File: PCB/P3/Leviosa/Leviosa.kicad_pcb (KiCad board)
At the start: 2 copper layers, 80 x 80 mm, 54 parts, among them J1 Barrel_Jack, J2 2.54mm 1x03 Spare

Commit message: create PCB initial draft
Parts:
- removed 0R1: DNP, Resistor_SMD:R_0603_1608Metric
- removed Q_noMag1: NCE0110K, Package_TO_SOT_SMD:TO-252-2
- removed R13: 1kΩ, Resistor_SMD:R_0805_2012Metric_Pad1.20x1.40mm_HandSolder
- removed R15: 0Ω, Resistor_SMD:R_0603_1608Metric
- removed TP_noMag1: no_magnet_point_trigger, TestPoint:TestPoint_Pad_D1.5mm
- removed hall_sensor1: SS495A, Connector_PinHeader_2.54mm:PinHeader_1x03_P2.54mm_Vertical
- added C5: 22µF, Capacitor_SMD:C_0805_2012Metric, F.Cu at (66.5, 111.1)
- added C6: 22µF, Capacitor_SMD:C_0805_2012Metric, F.Cu at (76.8, 111.1)
- added C_hall1: 4.7nF, Capacitor_SMD:C_0805_2012Metric_Pad1.18x1.45mm_HandSolder, F.Cu at (92.2, 65.7)
- added R14: 3.9kΩ, Resistor_SMD:R_0603_1608Metric, F.Cu at (92.8, 75.7)
- added R_brake1: 8.2Ω, Resistor_SMD:R_1206_3216Metric, F.Cu at (118.8, 71.7)
- added gate_driver1: MX27517, Package_TO_SOT_SMD:SOT-23-6, F.Cu at (100.5, 71.7)
- added hall1: SS495A, Connector_PinHeader_2.54mm:PinHeader_1x03_P2.54mm_Vertical, F.Cu at (81.2, 68.0)
- added opAmp1: MCP6001R, Package_TO_SOT_SMD:SOT-23-5, F.Cu at (87.0, 67.6)
- C1, C3: value 22µF -> 0.33µF
- Coil1: value 3.7mH -> 7.4mH; footprint Inductor_THT:L_Axial_L5.0mm_D3.6mm_P10.00mm_Horizontal_Murata_BL01RN1A2A2 -> Connector_PinHeader_2.54mm:PinHeader_2x01_P2.54mm_Vertical
- R4: value DNP -> 8.2Ω; footprint Resistor_SMD:R_0603_1608Metric -> Resistor_SMD:R_1206_3216Metric
- R5: footprint Resistor_SMD:R_0603_1608Metric -> Resistor_SMD:R_0805_2012Metric_Pad1.20x1.40mm_HandSolder
- R8: value 1kΩ -> 0Ω
- TP_12V1, TP_Fault1, TP_GND1, TP_Vout1, TP_coilOut1, TP_setPt1: footprint TestPoint:TestPoint_Pad_D1.5mm -> TestPoint:TestPoint_Pad_D1.0mm
- V_reg1: value AMS1117-5.0 -> MC7805BD2TR4G; footprint Package_TO_SOT_SMD:SOT-223-3_TabPin2 -> Package_TO_SOT_SMD:TO-263-2
- comparator1: footprint Package_SO:SOIC-8_5.3x5.3mm_P1.27mm -> Package_SO:SOIC-8_3.9x4.9mm_P1.27mm
- moved H3 140.8 mm to (222.8, 106.6)
- moved H2 138.6 mm to (222.8, 99.3)
- moved FID2 136.0 mm to (223.5, 119.8)
- moved FID3 104.2 mm to (223.5, 122.3)
- moved FID1 102.2 mm to (223.5, 117.2)
- moved H1 87.2 mm to (222.8, 92.1)
- moved TP_5V1 65.4 mm to (66.4, 90.4)
- moved R3 61.1 mm to (112.3, 76.2), turned to 0 degrees
- moved R4 60.1 mm to (91.9, 68.0)
- moved D2 57.1 mm to (108.5, 76.2)
- moved TP_Vout1 56.9 mm to (114.5, 80.1)
- moved D1 52.6 mm to (103.9, 75.6), turned to 0 degrees
- moved R5 48.7 mm to (104.2, 71.8), turned to -90 degrees
- moved TP_GND1 47.9 mm to (81.6, 114.5)
- moved C2 47.5 mm to (99.5, 75.7), turned to 90 degrees
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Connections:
- C_coil1 pad 1: Net-(D_coil1-K) -> /V_out
- Coil1 pad 1: Net-(D_coil1-K) -> /V_out
- Coil1 pad 2: /coil_output -> Net-(Coil1-Pad2)
- D_coil1 pad 1: Net-(D_coil1-K) -> /V_out
- D_coil1 pad 2: /coil_output -> Net-(D_coil1-A)
- Q_setPt1 pad 1: Net-(Q_setPt1-G) -> /gate_driver_out
- Q_setPt1 pad 3: /transistor1_output -> GND
- R10 pad 1: Net-(0R1-Pad1) -> Net-(Coil1-Pad2)
- R4 pad 1: Net-(current_sense1-REF) -> /instrumental_out
- R4 pad 2: /5V -> Net-(comparator1A-+)
- R5 pad 1: GND -> Net-(gate_driver1-OUT)
- R5 pad 2: Net-(current_sense1-REF) -> /gate_driver_out
- R8 pad 1: Net-(Q_setPt1-G) -> /comparator_out
- R8 pad 2: /set_point_trigger -> Net-(gate_driver1-IN+)
- R9 pad 1: /V_out -> /coil_output
- R_shunt1 pad 1: Net-(D_coil1-K) -> Net-(Coil1-Pad2)
- R_shunt1 pad 2: /V_out -> /coil_output
- Servo1 pad 2: GND -> /5V
- Servo1 pad 3: /5V -> GND
- Servo2 pad 2: GND -> /5V
- Servo2 pad 3: /5V -> GND
- TP_setPt1 pad 1: Net-(Q_setPt1-G) -> /gate_driver_out
- comparator1 pad 1: /set_point_trigger -> /comparator_out
- comparator1 pad 3: /hall_output -> Net-(comparator1A-+)
- comparator1 pad 6: /hall_output -> Net-(comparator1A-+)
- comparator1 pad 7: /no_magnet_point_trigger -> /comparator_out
- current_sense1 pad 1: Net-(current_sense1-REF) -> GND
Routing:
- net /current_sense: track 43.6 -> 90.8 mm
- net /V_out: track 83.5 -> 40.2 mm
- net /5V: track 162.5 -> 199.4 mm
- net /coil_output: track 56.6 -> 28.3 mm
- net /set_point: track 34.0 -> 10.1 mm
- net Net-(Q_noMag1-G): track 21.0 -> 0.00 mm
- net Net-(D_coil1-K): track 16.0 -> 0.00 mm
- net Net-(comparator1A-+): track 0.00 -> 12.6 mm
- net Net-(0R1-Pad1): track 12.5 -> 0.00 mm
- net Net-(current_lim1-DELAY): track 2.10 -> 14.2 mm
- net /hall_output: track 11.9 -> 0.00 mm
- net Net-(Q_setPt1-G): track 11.2 -> 0.00 mm
- net /gate_driver_out: track 0.00 -> 11.0 mm
- net /comparator_out: track 0.00 -> 10.1 mm
- net /no_magnet_point_trigger: track 9.37 -> 0.00 mm
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- removed copper zone on F.Cu, net +12V

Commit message: update PCB and schematic slightly
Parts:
- removed H3: MountingHole, MountingHole:MountingHole_3.2mm_M3_ISO7380
- moved FID3 159.2 mm to (66.8, 94.0)
- moved H2 146.1 mm to (80.0, 130.4)
- moved FID1 142.9 mm to (80.7, 112.7)
- moved FID2 106.8 mm to (121.4, 88.5)
- moved H1 90.2 mm to (132.9, 84.4)
- moved GND1 16.7 mm to (66.5, 107.4)
- moved MCU1 8.60 mm to (76.3, 128.1), turned to 135 degrees
- moved C_MCU1 8.09 mm to (69.7, 119.8), turned to 0 degrees
- moved J2 5.83 mm to (86.2, 120.4), turned to -135 degrees
- moved fault1 1.03 mm to (80.7, 85.3)
- moved C_hall1 0.90 mm to (92.1, 64.8)
- moved R4 0.90 mm to (91.8, 67.1)
- moved Vout1 0.61 mm to (113.9, 80.0)
- moved coilOut1 0.30 mm to (115.4, 69.0)
- renumbered TP_12V1 to 12V1, TP_5V1 to 5V1, Cbypass2 to C_MCU1, Cbypass1 to C_sense1, TP_GND1 to GND1, Q_setPt1 to Q1, Servo1 to Srvo1, Servo2 to Srvo2, current_lim1 to U_Ilim1, current_sense1 to U_sense1, TP_Vout1 to Vout1, comparator1 to cmprtr1, TP_coilOut1 to coilOut1, TP_Fault1 to fault1, gate_driver1 to gtDrvr1, TP_setPt1 to gtOut1, Pot_setPt1 to pot1
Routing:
- net GND: track 16.0 -> 32.8 mm, vias 0 -> 13
- net /PB3: track 4.73 -> 11.1 mm
- net /5V: track 199.4 -> 193.7 mm
- net /V_out: track 40.2 -> 44.3 mm
- net /PB4: track 4.73 -> 8.46 mm
- net /servo1_control: track 9.72 -> 6.79 mm
- net Net-(D_coil1-A): track 0.00 -> 2.79 mm
- net /PB5: track 16.1 -> 13.9 mm
- net /current_sense: track 90.8 -> 92.2 mm
- net /instrumental_out: track 5.76 -> 6.84 mm
- net Net-(cmprtr1A-+): track 12.6 -> 13.5 mm
- net /servo2_control: track 4.59 -> 3.76 mm
- added copper zone on F.Cu, net /coil_output
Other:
- board size 80 x 80 mm -> 78.2 x 75.4 mm

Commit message: Board revised
- Big change from the last so have a look over
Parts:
- removed C_MCU1, C_sense1: 0.1µF, Capacitor_SMD:C_0402_1005Metric
- removed C_coil1: 20nF, Capacitor_SMD:C_0805_2012Metric_Pad1.18x1.45mm_HandSolder
- removed C_hall1: 4.7nF, Capacitor_SMD:C_0805_2012Metric_Pad1.18x1.45mm_HandSolder
- removed Coil1: 7.4mH, Connector_PinHeader_2.54mm:PinHeader_2x01_P2.54mm_Vertical
- removed D_coil1: SS34, Diode_SMD:D_SMA
- removed R_brake1: 8.2Ω, Resistor_SMD:R_1206_3216Metric
- removed R_shunt1: 50mΩ, Resistor_SMD:R_2010_5025Metric
- removed Srvo1, Srvo2: 2.54mm 1x03 Servo 1, Connector_PinHeader_2.54mm:PinHeader_1x03_P2.54mm_Vertical
- removed U_Ilim1: TPS1H200AQDGNRQ1, TPS1H200AQDGNRQ1:SOP65P490X110-9N
- removed U_sense1: INA199xxDCK (50V/V), Package_TO_SOT_SMD:SOT-363_SC-70-6
- removed V_reg1: MC7805BD2TR4G, Package_TO_SOT_SMD:TO-263-2
- removed Vout1: Vout, TestPoint:TestPoint_Pad_D1.0mm
- removed cmprtr1: LM393, Package_SO:SOIC-8_3.9x4.9mm_P1.27mm
- removed coilOut1: coil_out, TestPoint:TestPoint_Pad_D1.0mm
- removed fault1: Fault, TestPoint:TestPoint_Pad_D1.0mm
- removed gtDrvr1: MX27517, Package_TO_SOT_SMD:SOT-23-6
- removed gtOut1: set_point_trigger, TestPoint:TestPoint_Pad_D1.0mm
- removed hall1: SS495A, Connector_PinHeader_2.54mm:PinHeader_1x03_P2.54mm_Vertical
- removed opAmp1: MCP6001R, Package_TO_SOT_SMD:SOT-23-5
- added C10: 47μF, Capacitor_SMD:C_1206_3216Metric, F.Cu at (113.0, 76.9)
- added C11: 0.1µF, Capacitor_SMD:C_0603_1608Metric, F.Cu at (120.1, 77.7)
- added C7: 0.1uF, Capacitor_SMD:C_0603_1608Metric, F.Cu at (133.5, 104.8)
- added C8: 4.7nF, Capacitor_SMD:C_0805_2012Metric_Pad1.18x1.45mm_HandSolder, F.Cu at (129.5, 104.8)
- added C9: 20nF, Capacitor_SMD:C_0805_2012Metric_Pad1.18x1.45mm_HandSolder, F.Cu at (95.9, 69.2)
- added D3: SS34, Diode_SMD:D_SOD-323, F.Cu at (95.9, 72.7)
- added G1: set_point_trigger, TestPoint:TestPoint_Pad_D1.0mm, F.Cu at (114.3, 66.0)
- added L1: 7.4mH, Connector_PinHeader_2.54mm:PinHeader_2x01_P2.54mm_Vertical, F.Cu at (98.4, 76.2)
- added R13: 8.2Ω, Resistor_SMD:R_1206_3216Metric, F.Cu at (109.2, 78.1)
- added R15: 0Ω, Resistor_SMD:R_0603_1608Metric, F.Cu at (114.3, 68.6)
- added SRV1: 2.54mm 1x03 Servo 1, Connector_PinHeader_2.54mm:PinHeader_1x03_P2.54mm_Vertical, F.Cu at (85.7, 129.8)
- added SRV2: 2.54mm 1x03 Servo 1, Connector_PinHeader_2.54mm:PinHeader_1x03_P2.54mm_Vertical, F.Cu at (80.6, 123.2)
- added TP_COIL1: Coil Output, TestPoint:TestPoint_Pad_D1.0mm, F.Cu at (107.3, 71.1)
- added TP_F1: Fault, TestPoint:TestPoint_Pad_D1.0mm, F.Cu at (82.5, 69.2)
- added U1: TPS1H200AQDGNRQ1, TPS1H200AQDGNRQ1:SOP65P490X110-9N, F.Cu at (90.1, 75.9)
- added U2: MC7805BD2TR4G, Package_TO_SOT_SMD:TO-263-2, F.Cu at (69.8, 96.3)
- added U3: SS495A, Connector_PinHeader_2.54mm:PinHeader_1x03_P2.54mm_Vertical, F.Cu at (137.2, 102.7)
- added U4: MCP6001R, Package_TO_SOT_SMD:SOT-23-5, F.Cu at (132.7, 97.5)
- added U5: LM393, Package_SO:SOIC-8_3.9x4.9mm_P1.27mm, F.Cu at (127.0, 99.7)
- added U6: MX27517, Package_TO_SOT_SMD:SOT-23-6, F.Cu at (114.3, 71.7)
- added U7: INA199xxDCK (50V/V), Package_TO_SOT_SMD:SOT-363_SC-70-6, F.Cu at (116.1, 77.8)
- added VO1: Vout, TestPoint:TestPoint_Pad_D1.0mm, F.Cu at (92.1, 72.4)
- C1: value 0.33µF -> 22µF
- C2: value 22µF -> 0.33µF
- C3: value 0.33µF -> 0.1µF; footprint Capacitor_SMD:C_0805_2012Metric -> Capacitor_SMD:C_0603_1608Metric
- C4: value 47μF -> 0.33µF; footprint Capacitor_SMD:C_1206_3216Metric -> Capacitor_SMD:C_0805_2012Metric
- R1, R3: footprint Resistor_SMD:R_0805_2012Metric_Pad1.20x1.40mm_HandSolder -> Resistor_SMD:R_0603_1608Metric
- R11: value 68kΩ -> 50mΩ; footprint Resistor_SMD:R_0603_1608Metric -> Resistor_SMD:R_2010_5025Metric
- R12: value 3.9kΩ -> 0Ω
- R14: value 3.9kΩ -> 8.2Ω; footprint Resistor_SMD:R_0603_1608Metric -> Resistor_SMD:R_1206_3216Metric
- R4: value 8.2Ω -> 51kΩ; footprint Resistor_SMD:R_1206_3216Metric -> Resistor_SMD:R_0603_1608Metric
- R5: value 0Ω -> 3.9kΩ; footprint Resistor_SMD:R_0805_2012Metric_Pad1.20x1.40mm_HandSolder -> Resistor_SMD:R_0603_1608Metric
- R6: value 51kΩ -> 100kΩ
- R7: value 100kΩ -> 68kΩ; footprint Resistor_SMD:R_0805_2012Metric_Pad1.20x1.40mm_HandSolder -> Resistor_SMD:R_0603_1608Metric
- R8: value 0Ω -> 8.2Ω; footprint Resistor_SMD:R_0805_2012Metric_Pad1.20x1.40mm_HandSolder -> Resistor_SMD:R_1206_3216Metric
- R9: value 8.2Ω -> 3.9kΩ; footprint Resistor_SMD:R_1206_3216Metric -> Resistor_SMD:R_0603_1608Metric
- moved FID3 67.1 mm to (133.1, 83.8)
- moved pot1 60.6 mm to (135.3, 114.3), turned to 180 degrees
- moved H1 60.5 mm to (97.0, 133.1)
- moved R4 59.0 mm to (129.5, 112.4), turned to 180 degrees
- moved C4 53.5 mm to (76.8, 101.0), turned to 90 degrees
- moved R5 49.7 mm to (129.5, 114.6), turned to 0 degrees
- moved FID2 49.7 mm to (109.2, 136.7)
- moved R7 47.9 mm to (128.9, 92.7), turned to 180 degrees
- moved R8 46.4 mm to (132.7, 102.2), turned to 180 degrees
- moved R6 45.6 mm to (128.9, 94.6), turned to 0 degrees
- moved H2 43.7 mm to (121.7, 117.3)
- moved C3 36.8 mm to (64.8, 105.8), turned to -90 degrees
- moved C2 34.8 mm to (65.9, 84.9), turned to 0 degrees
- moved FID1 34.6 mm to (68.6, 80.3)
- moved C1 29.2 mm to (94.6, 75.9), turned to -90 degrees
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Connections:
- 5V1 pad 1: /5V -> +5V
- C1 pad 1: +12V -> +12V_SF
- C2 pad 1: /V_out -> +12V
- C3 pad 1: /5V -> +5V
- C4 pad 1: Net-(U_sense1-+) -> +5V
- C4 pad 2: Net-(U_sense1--) -> GND
- C5 pad 1: /5V -> +5V
- C6 pad 1: /5V -> +5V
- D1 pad 1: /V_out -> +12V_SF
- MCU1 pad 5: /servo2_control -> /SVR2_CTRL
- MCU1 pad 6: /servo1_control -> /SVR1_CTRL
- MCU1 pad 7: /current_sense -> /CURT_SN
- MCU1 pad 8: /5V -> +5V
- Q1 pad 1: /gate_driver_out -> /GT_DRV
- Q1 pad 2: /coil_output -> /COIL_OUT
- R10 pad 2: Net-(U_sense1--) -> /COIL_OUT
- R11 pad 1: GND -> Net-(L1-Pad2)
- R11 pad 2: /no_magnet_point -> /COIL_OUT
- R12 pad 1: GND -> /COMP_OUT
- R12 pad 2: Net-(R12-Pad2) -> Net-(U6-IN+)
- R14 pad 1: /comparator_out -> /COIL_OUT
- R14 pad 2: /5V -> Net-(U7-+)
- R4 pad 1: /instrumental_out -> Net-(R4-Pad1)
- R4 pad 2: Net-(cmprtr1A-+) -> +5V
- R5 pad 1: Net-(gtDrvr1-OUT) -> GND
- R5 pad 2: /gate_driver_out -> Net-(R5-Pad2)
- R6 pad 1: Net-(R6-Pad1) -> /NO_MGNT_PT
- R6 pad 2: /5V -> +5V
- R7 pad 1: /no_magnet_point -> GND
- R7 pad 2: /5V -> /NO_MGNT_PT
- R8 pad 1: /comparator_out -> /INST_OUT
- R9 pad 1: /coil_output -> /COMP_OUT
- R9 pad 2: Net-(U_sense1-+) -> +5V
- pot1 pad 1: Net-(R12-Pad2) -> Net-(R5-Pad2)
- pot1 pad 2: /set_point -> /SET_PT
- pot1 pad 3: Net-(R6-Pad1) -> Net-(R4-Pad1)
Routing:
- net +5V: track 0.00 -> 215.3 mm, vias 0 -> 11
- net /5V: track 193.7 -> 0.00 mm
- net /CURT_SN: track 0.00 -> 96.7 mm
- net /current_sense: track 92.2 -> 0.00 mm
- net /V_out: track 44.3 -> 0.00 mm
- net /COMP_OUT: track 0.00 -> 32.8 mm
- net /SVR2_CTRL: track 0.00 -> 30.5 mm, vias 0 -> 4
- net GND: track 32.8 -> 2.57 mm, vias 13 -> 24
- net /coil_output: track 28.3 -> 0.00 mm
- net +12V_SF: track 0.00 -> 25.2 mm
- net /SVR1_CTRL: track 0.00 -> 23.7 mm, vias 0 -> 4
- net /COIL_OUT: track 0.00 -> 22.4 mm
- net Net-(cmprtr1A-+): track 13.5 -> 0.00 mm
- net /SET_PT: track 0.00 -> 12.3 mm
- net Net-(U1-~{FAULT}): track 0.00 -> 12.1 mm, vias 0 -> 2
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- removed copper zone on F.Cu, net /coil_output
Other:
- board size 78.2 x 75.4 mm -> 80 x 80 mm

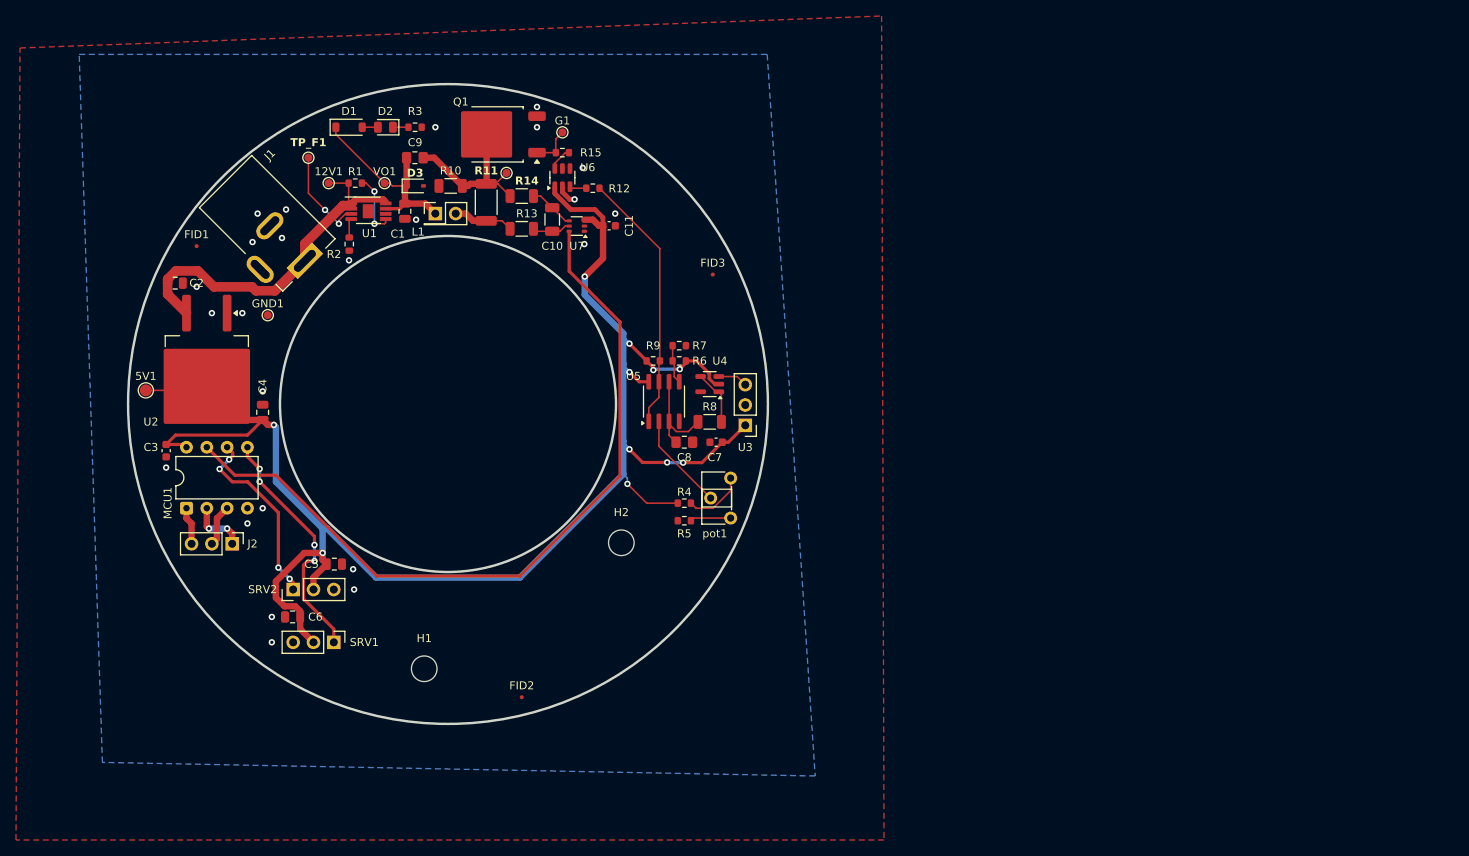
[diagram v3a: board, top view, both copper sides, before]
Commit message: added status led for coil and moved components groups closer together
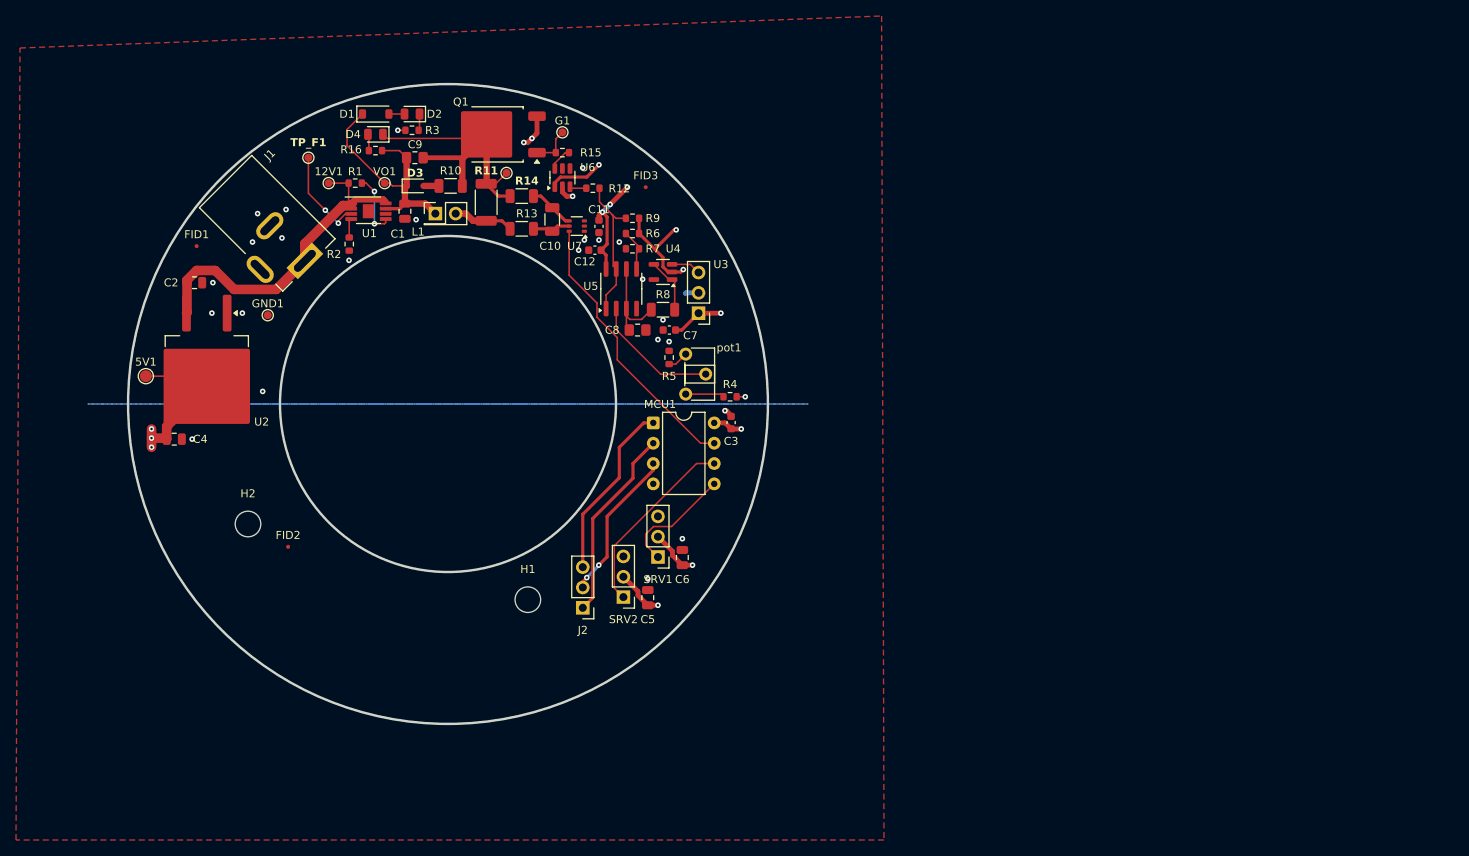
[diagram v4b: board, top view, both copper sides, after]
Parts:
- added C12: 0.1uF, Capacitor_SMD:C_0603_1608Metric, F.Cu at (118.4, 80.8)
- added D4: LED, LED_SMD:LED_0805_2012Metric, F.Cu at (90.9, 66.3)
- added R16: 2kΩ, Resistor_SMD:R_0603_1608Metric, F.Cu at (90.9, 68.3)
- moved C3 70.7 mm to (135.4, 102.3), turned to 90 degrees
- moved MCU1 59.3 mm to (125.7, 102.4), turned to 0 degrees
- moved C6 49.3 mm to (129.3, 119.2), turned to 90 degrees
- moved H2 46.7 mm to (75.0, 115.0)
- moved J2 44.5 mm to (116.8, 125.5), turned to 180 degrees
- moved SRV1 41.9 mm to (126.2, 119.1), turned to 180 degrees
- moved SRV2 41.3 mm to (121.9, 124.1), turned to 180 degrees
- moved C5 39.4 mm to (125.0, 124.2), turned to 90 degrees
- moved FID2 34.7 mm to (80.0, 117.9)
- moved pot1 21.3 mm to (129.7, 93.8), turned to 0 degrees
- moved R5 20.5 mm to (127.6, 94.2), turned to -90 degrees
- moved R9 18.0 mm to (123.1, 76.8), turned to 0 degrees
- moved R6 17.0 mm to (123.1, 78.7)
- moved H1 15.6 mm to (110.0, 124.5)
- moved C8 15.2 mm to (123.7, 90.8)
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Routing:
- net +5V: track 215.3 -> 84.9 mm, vias 11 -> 14
- net /CURT_SN: track 96.7 -> 35.0 mm
- net /COIL_OUT: track 22.4 -> 43.1 mm
- net /PB5: track 4.71 -> 22.4 mm
- net /PB3: track 7.10 -> 24.2 mm, vias 2 -> 0
- net /SVR2_CTRL: track 30.5 -> 14.6 mm, vias 4 -> 0
- net /COMP_OUT: track 32.8 -> 18.3 mm
- net /PB4: track 5.24 -> 19.1 mm, vias 0 -> 2
- net GND: track 2.57 -> 10.2 mm, vias 24 -> 27
- net +12V_SF: track 25.2 -> 30.5 mm
- net /SET_PT: track 12.3 -> 16.1 mm
- net +12V: track 45.1 -> 41.6 mm
- net Net-(R4-Pad1): track 7.71 -> 4.86 mm
- net Net-(R5-Pad2): track 5.11 -> 2.59 mm
- net Net-(D4-A): track 0.00 -> 2.08 mm
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- added copper zone on B.Cu, net +5V
